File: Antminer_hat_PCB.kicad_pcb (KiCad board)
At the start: 2 copper layers, 100 x 81 mm, 65 parts, among them IC1 USB3315C-CP-TR, IC2 LM3525M-H, J1 Conn_02x09_Odd_Even, J11 Aux_mio_conn, J12 12v Pwr, J13 HDMI_A, J14 USB_C_Receptacle_USB2.0_16P, J15 48204-0001 China, J16 PL_conn, J2 Conn_02x09_Odd_Even, J3 Conn_02x09_Odd_Even, J4 Conn_02x09_Odd_Even, J5 Conn_02x09_Odd_Even, J6 Conn_02x09_Odd_Even, J7 Conn_02x09_Odd_Even, J8 Conn_02x09_Odd_Even, J9 Conn_02x09_Odd_Even, U1 L7805, U2 LM1117DT-1.8, Y1 24Mhz

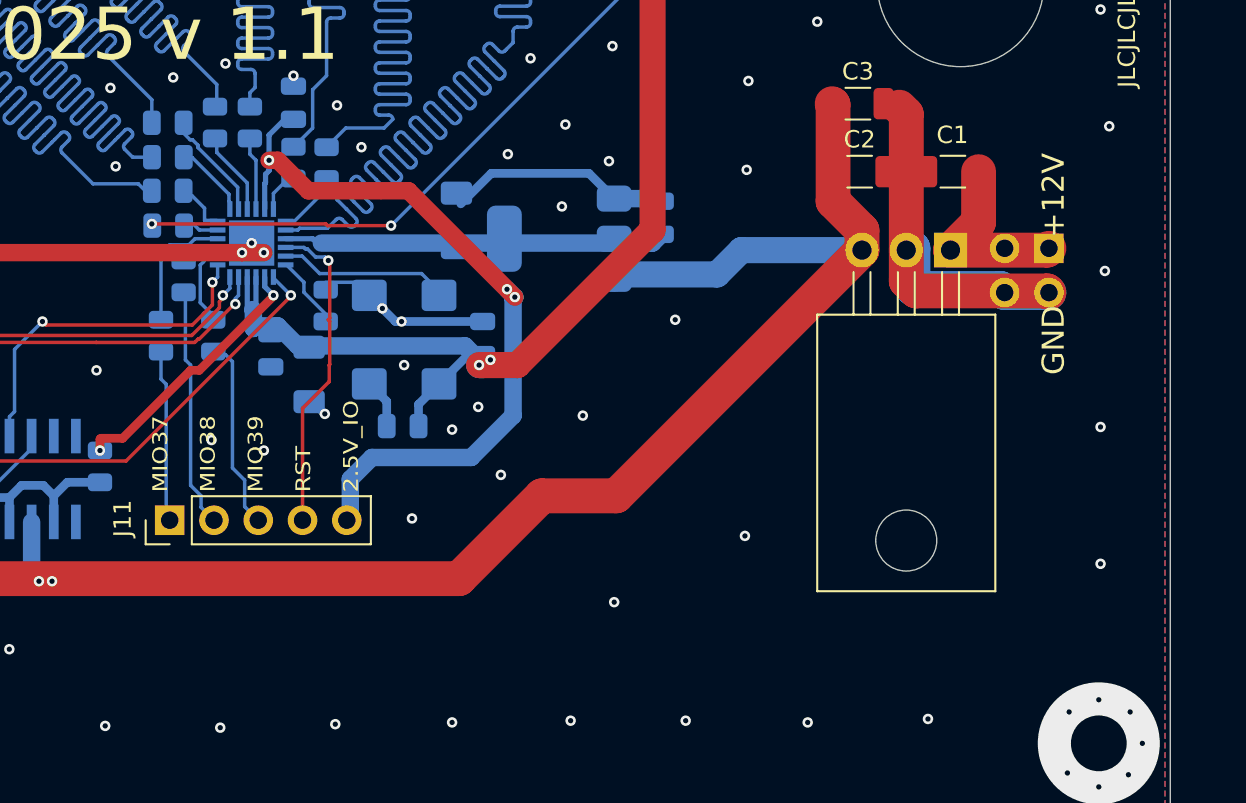
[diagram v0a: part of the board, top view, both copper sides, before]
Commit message: - Updated schematic to use correct type of external connectors
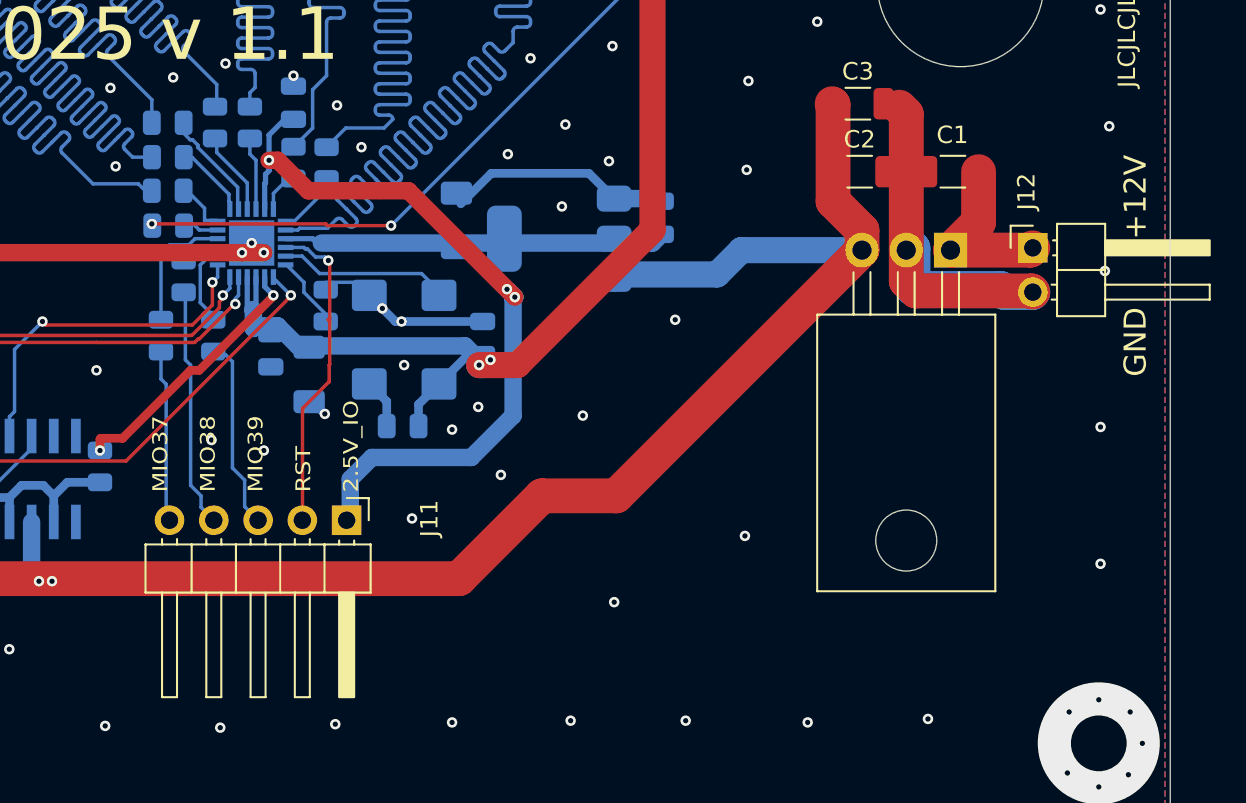
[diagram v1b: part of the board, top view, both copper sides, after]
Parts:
- J11: footprint Connector_PinHeader_2.54mm:PinHeader_1x05_P2.54mm_Vertical -> Connector_PinHeader_2.54mm:PinHeader_1x05_P2.54mm_Horizontal
- J12: footprint Connector_PinSocket_2.54mm:PinSocket_2x02_P2.54mm_Vertical -> Connector_PinHeader_2.54mm:PinHeader_1x02_P2.54mm_Horizontal; moved to F.Cu
- moved J11 10.2 mm to (77.8, 105.1), turned to -90 degrees
- moved J12 0.93 mm to (117.1, 89.5), turned to 0 degrees
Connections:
- J1 pad 16: +3.3V -> unconnected-(J1-Pin_16-Pad16)
- J11 pad 1: DATA5 -> 2.5VCC_IO
- J11 pad 2: DATA6 -> RST
- J11 pad 4: RST -> DATA6
- J11 pad 5: 2.5VCC_IO -> DATA5
- J8 pad 16: +3.3V -> unconnected-(J8-Pin_16-Pad16)
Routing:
- net GND: track 257.0 -> 255.2 mm
- net +12V: track 10.9 -> 9.94 mm
